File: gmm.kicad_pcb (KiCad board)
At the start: 6 copper layers, 55 x 50 mm, 14 parts, among them P1 10144518-101802LF, P2 10144518-061802LF, P3 10144518-061802LF, P4 10144518-061802LF, U1 CCGM1A1, U2 5P49V6965, U3 LM26480SQ, Y1 NX3225SA

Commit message: FPGA core and IO power, PLL and SERDES, FPGA GPIO signals are connected... WIP
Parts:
- added C10: 0.01uF, Capacitor_SMD:C_0402_1005Metric, F.Cu at (156.8, 171.9)
- added C11: 0.01uF, Capacitor_SMD:C_0402_1005Metric, F.Cu at (168.9, 161.9)
- added C12: 1.0uF, Capacitor_SMD:C_0603_1608Metric, F.Cu at (157.4, 164.7)
- added C13: 0.1uF, Capacitor_SMD:C_0402_1005Metric, F.Cu at (163.8, 166.9)
- added C14: 0.1uF, Capacitor_SMD:C_0402_1005Metric, F.Cu at (160.8, 168.9)
- added C15: 1.0uF, Capacitor_SMD:C_0603_1608Metric, F.Cu at (157.4, 162.2)
- added C16: 0.01uF, Capacitor_SMD:C_0402_1005Metric, F.Cu at (160.8, 170.9)
- added C17: 0.01uF, Capacitor_SMD:C_0402_1005Metric, F.Cu at (167.8, 164.4)
- added C18: 1.0uF, Capacitor_SMD:C_0603_1608Metric, F.Cu at (153.4, 162.2)
- added C19: 0.1uF, Capacitor_SMD:C_0402_1005Metric, F.Cu at (166.7, 168.4)
- added C20: 0.1uF, Capacitor_SMD:C_0402_1005Metric, F.Cu at (164.8, 164.4)
- added C21: 0.1uF, Capacitor_SMD:C_0402_1005Metric, F.Cu at (169.6, 171.8)
- added C22: 1.0uF, Capacitor_SMD:C_0603_1608Metric, F.Cu at (153.4, 156.2)
- added C23: 0.01uF, Capacitor_SMD:C_0402_1005Metric, F.Cu at (168.9, 145.9)
- added C24: 0.01uF, Capacitor_SMD:C_0402_1005Metric, F.Cu at (160.8, 153.5)
- added C25: 0.01uF, Capacitor_SMD:C_0402_1005Metric, F.Cu at (176.9, 138.4)
- added C26: 0.01uF, Capacitor_SMD:C_0402_1005Metric, F.Cu at (156.8, 156.0)
- added C27: 0.01uF, Capacitor_SMD:C_0402_1005Metric, F.Cu at (164.8, 148.5)
- added C28: 0.01uF, Capacitor_SMD:C_0402_1005Metric, F.Cu at (172.5, 152.9)
- added C29: 0.01uF, Capacitor_SMD:C_0402_1005Metric, F.Cu at (185.2, 146.4)
- added C3: 0.1uF, Capacitor_SMD:C_0402_1005Metric, F.Cu at (172.5, 167.9)
- added C30: 0.01uF, Capacitor_SMD:C_0402_1005Metric, F.Cu at (174.3, 156.8)
- added C31: 1.0uF, Capacitor_SMD:C_0603_1608Metric, F.Cu at (157.4, 153.7)
- added C32: 1.0uF, Capacitor_SMD:C_0603_1608Metric, F.Cu at (169.4, 143.7)
- added C33: 0.01uF, Capacitor_SMD:C_0402_1005Metric, F.Cu at (178.3, 152.9)
- added C34: 0.01uF, Capacitor_SMD:C_0402_1005Metric, F.Cu at (184.5, 142.4)
- added C35: 0.01uF, Capacitor_SMD:C_0402_1005Metric, F.Cu at (182.3, 148.4)
- added C36: 0.01uF, Capacitor_SMD:C_0402_1005Metric, F.Cu at (179.4, 150.4)
- added C37: 0.01uF, Capacitor_SMD:C_0402_1005Metric, F.Cu at (171.4, 156.8)
- added C38: 0.01uF, Capacitor_SMD:C_0402_1005Metric, F.Cu at (172.9, 140.9)
- added C39: 0.01uF, Capacitor_SMD:C_0402_1005Metric, F.Cu at (184.5, 144.4)
- added C4: 1.0uF, Capacitor_SMD:C_0603_1608Metric, F.Cu at (161.4, 162.2)
- added C40: 0.01uF, Capacitor_SMD:C_0402_1005Metric, F.Cu at (175.4, 152.9)
- added C41: 1.0uF, Capacitor_SMD:C_0603_1608Metric, F.Cu at (153.4, 151.2)
- added C42: 1.0uF, Capacitor_SMD:C_0603_1608Metric, F.Cu at (165.4, 141.2)
- added C43: 0.01uF, Capacitor_SMD:C_0402_1005Metric, F.Cu at (176.5, 150.9)
- added C44: 0.01uF, Capacitor_SMD:C_0402_1005Metric, F.Cu at (172.5, 154.9)
- added C45: 0.01uF, Capacitor_SMD:C_0402_1005Metric, F.Cu at (175.4, 154.9)
- added C46: 0.01uF, Capacitor_SMD:C_0402_1005Metric, F.Cu at (179.4, 146.4)
- added C47: 0.01uF, Capacitor_SMD:C_0402_1005Metric, F.Cu at (175.8, 142.9)
- added C48: 0.01uF, Capacitor_SMD:C_0402_1005Metric, F.Cu at (178.7, 142.4)
- added C49: 0.01uF, Capacitor_SMD:C_0402_1005Metric, F.Cu at (166.7, 154.4)
- added C5: 0.01uF, Capacitor_SMD:C_0402_1005Metric, F.Cu at (170.7, 163.9)
- added C50: 0.01uF, Capacitor_SMD:C_0402_1005Metric, F.Cu at (182.7, 138.4)
- added C51: 1.0uF, Capacitor_SMD:C_0603_1608Metric, F.Cu at (165.4, 146.2)
- added C52: 1.0uF, Capacitor_SMD:C_0603_1608Metric, F.Cu at (161.4, 151.2)
- added C53: 0.01uF, Capacitor_SMD:C_0402_1005Metric, F.Cu at (166.7, 152.4)
- added C54: 0.01uF, Capacitor_SMD:C_0402_1005Metric, F.Cu at (178.7, 140.4)
- added C55: 0.01uF, Capacitor_SMD:C_0402_1005Metric, F.Cu at (170.7, 147.9)
- added C56: 0.01uF, Capacitor_SMD:C_0402_1005Metric, F.Cu at (162.7, 155.5)
- added C57: 0.01uF, Capacitor_SMD:C_0402_1005Metric, F.Cu at (167.8, 150.4)
- added C58: 0.01uF, Capacitor_SMD:C_0402_1005Metric, F.Cu at (172.9, 142.9)
- added C59: 0.01uF, Capacitor_SMD:C_0402_1005Metric, F.Cu at (172.9, 144.9)
- added C6: 0.01uF, Capacitor_SMD:C_0402_1005Metric, F.Cu at (166.7, 166.4)
- added C60: 0.01uF, Capacitor_SMD:C_0402_1005Metric, F.Cu at (179.8, 138.4)
- added C61: 1.0uF, Capacitor_SMD:C_0603_1608Metric, F.Cu at (157.4, 143.7)
- added C62: 0.01uF, Capacitor_SMD:C_0402_1005Metric, F.Cu at (163.8, 153.5)
- added C63: 0.01uF, Capacitor_SMD:C_0402_1005Metric, F.Cu at (175.8, 140.9)
- added C64: 0.01uF, Capacitor_SMD:C_0402_1005Metric, F.Cu at (164.8, 150.4)
- added C65: 0.01uF, Capacitor_SMD:C_0402_1005Metric, F.Cu at (167.8, 148.5)
- added C66: 1.0uF, Capacitor_SMD:C_0603_1608Metric, F.Cu at (169.4, 138.7)
- added C67: 1.0uF, Capacitor_SMD:C_0603_1608Metric, F.Cu at (153.4, 153.7)
- added C68: 1.0uF, Capacitor_SMD:C_0603_1608Metric, F.Cu at (161.4, 146.2)
- added C69: 1.0uF, Capacitor_SMD:C_0603_1608Metric, F.Cu at (157.4, 148.7)
- added C7: 0.01uF, Capacitor_SMD:C_0402_1005Metric, F.Cu at (171.8, 161.9)
- added C70: 1.0uF, Capacitor_SMD:C_0603_1608Metric, F.Cu at (157.4, 146.2)
- added C71: 0.1uF, Capacitor_SMD:C_0402_1005Metric, F.Cu at (159.7, 156.0)
- added C72: 1.0uF, Capacitor_SMD:C_0603_1608Metric, F.Cu at (161.4, 148.7)
- added C73: 0.01uF, Capacitor_SMD:C_0402_1005Metric, F.Cu at (179.4, 148.4)
- added C74: 0.01uF, Capacitor_SMD:C_0402_1005Metric, F.Cu at (168.5, 156.4)
- added C75: 0.01uF, Capacitor_SMD:C_0402_1005Metric, F.Cu at (184.5, 140.4)
- added C76: 0.01uF, Capacitor_SMD:C_0402_1005Metric, F.Cu at (165.6, 156.4)
- added C77: 0.01uF, Capacitor_SMD:C_0402_1005Metric, F.Cu at (178.7, 144.4)
- added C78: 0.1uF, Capacitor_SMD:C_0402_1005Metric, F.Cu at (173.6, 148.9)
- added C79: 1.0uF, Capacitor_SMD:C_0603_1608Metric, F.Cu at (169.4, 141.2)
- added C8: 0.1uF, Capacitor_SMD:C_0402_1005Metric, F.Cu at (160.8, 166.9)
- added C80: 0.01uF, Capacitor_SMD:C_0402_1005Metric, F.Cu at (169.6, 152.4)
- added C81: 0.01uF, Capacitor_SMD:C_0402_1005Metric, F.Cu at (185.6, 138.4)
- added C82: 0.01uF, Capacitor_SMD:C_0402_1005Metric, F.Cu at (170.7, 149.9)
- added C83: 0.01uF, Capacitor_SMD:C_0402_1005Metric, F.Cu at (181.6, 142.4)
- added C84: 0.01uF, Capacitor_SMD:C_0402_1005Metric, F.Cu at (176.5, 146.9)
- added C85: 0.1uF, Capacitor_SMD:C_0402_1005Metric, F.Cu at (173.6, 150.9)
- added C86: 1.0uF, Capacitor_SMD:C_0603_1608Metric, F.Cu at (173.4, 138.7)
- added C87: 0.01uF, Capacitor_SMD:C_0402_1005Metric, F.Cu at (176.5, 148.9)
- added C88: 0.01uF, Capacitor_SMD:C_0402_1005Metric, F.Cu at (181.6, 144.4)
- added C89: 0.01uF, Capacitor_SMD:C_0402_1005Metric, F.Cu at (182.3, 146.4)
- added C9: 1.0uF, Capacitor_SMD:C_0603_1608Metric, F.Cu at (153.4, 164.7)
- added C90: 0.01uF, Capacitor_SMD:C_0402_1005Metric, F.Cu at (181.6, 140.4)
- added C91: 0.01uF, Capacitor_SMD:C_0402_1005Metric, F.Cu at (169.6, 154.4)
- added C92: 0.1uF, Capacitor_SMD:C_0402_1005Metric, F.Cu at (175.8, 144.9)
- added C93: 1.0uF, Capacitor_SMD:C_0603_1608Metric, F.Cu at (161.4, 143.7)
- added C94: 0.01uF, Capacitor_SMD:C_0402_1005Metric, F.Cu at (173.6, 146.9)
- added L1: 4.7uH, Inductor_SMD:L_0603_1608Metric, F.Cu at (153.4, 167.2)
- added L2: 4.7uH, Inductor_SMD:L_0603_1608Metric, F.Cu at (157.4, 169.7)
- added L3: 4.7uH, Inductor_SMD:L_0603_1608Metric, F.Cu at (165.4, 162.2)
- added L4: 4.7uH, Inductor_SMD:L_0603_1608Metric, F.Cu at (153.4, 172.2)
- added L5: 4.7uH, Inductor_SMD:L_0603_1608Metric, F.Cu at (161.4, 164.7)
- added L6: 4.7uH, Inductor_SMD:L_0603_1608Metric, F.Cu at (153.4, 148.7)
- added L7: 4.7uH, Inductor_SMD:L_0603_1608Metric, F.Cu at (161.4, 141.2)
- added L8: 4.7uH, Inductor_SMD:L_0603_1608Metric, F.Cu at (157.4, 151.2)
- added L9: 4.7uH, Inductor_SMD:L_0603_1608Metric, F.Cu at (153.4, 146.2)
- added R1: DNI, Resistor_SMD:R_0603_1608Metric, F.Cu at (157.4, 167.2)
- added R10: DNI, Resistor_SMD:R_0603_1608Metric, F.Cu at (161.4, 138.7)
- added R11: DNI, Resistor_SMD:R_0603_1608Metric, F.Cu at (157.4, 141.2)
- added R12: DNI, Resistor_SMD:R_0603_1608Metric, F.Cu at (153.4, 143.7)
- added R13: DNI, Resistor_SMD:R_0603_1608Metric, F.Cu at (157.4, 138.7)
- added R14: DNI, Resistor_SMD:R_0603_1608Metric, F.Cu at (153.4, 141.2)
- added R15: DNI, Resistor_SMD:R_0603_1608Metric, F.Cu at (165.4, 138.7)
- added R16: DNI, Resistor_SMD:R_0603_1608Metric, F.Cu at (165.4, 143.7)
- added R17: DNI, Resistor_SMD:R_0603_1608Metric, F.Cu at (153.4, 138.7)
- added R2: DNI, Resistor_SMD:R_0603_1608Metric, F.Cu at (153.4, 169.7)
- added R3: 33, Resistor_SMD:R_0402_1005Metric, F.Cu at (163.8, 168.9)
- added R4: 100, Resistor_SMD:R_0402_1005Metric, F.Cu at (163.8, 170.9)
- added R5: 10k, Resistor_SMD:R_0402_1005Metric, F.Cu at (170.7, 165.9)
- added R6: DNI, Resistor_SMD:R_0402_1005Metric, F.Cu at (166.7, 170.4)
- added R7: 200, Resistor_SMD:R_0402_1005Metric, F.Cu at (169.6, 167.9)
- added R8: 10k, Resistor_SMD:R_0402_1005Metric, F.Cu at (169.6, 169.9)
- added R9: 10k, Resistor_SMD:R_0402_1005Metric, F.Cu at (166.7, 172.4)
- MH1, MH2, MH3, MH4: footprint Mounting_Holes:MountingHole_2.7mm_M2.5_ISO14580_Pad -> MountingHole:MountingHole_2.7mm_M2.5_ISO14580_Pad
- P1: value 10144518-101802LF -> 10144518-061802LF; footprint Amphenol:10144518-101802LF -> Amphenol:10144518-061802LF; moved to F.Cu
- P2, P3: moved to F.Cu
- P4: value 10144518-061802LF -> 10144518-101802LF; footprint Amphenol:10144518-061802LF -> Amphenol:10144518-101802LF; moved to F.Cu
- U2: footprint Housings_DFN_QFN:QFN-24-1EP_4x4mm_Pitch0.5mm -> Package_DFN_QFN:QFN-24-1EP_4x4mm_P0.5mm_EP2.8x2.8mm_ThermalVias
- moved MH2 113.2 mm to (88.0, 182.5)
- moved MH1 106.3 mm to (88.0, 188.5)
- moved MH3 85.9 mm to (82.0, 188.5)
- moved P2 69.8 mm to (128.5, 153.3)
- moved P3 66.4 mm to (95.5, 153.3), turned to 0 degrees
- moved MH4 58.7 mm to (82.0, 182.5)
- moved P1 58.1 mm to (95.5, 163.7), turned to 0 degrees
- moved P4 23.7 mm to (103.4, 143.0), turned to 0 degrees
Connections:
- U1 pad A2: (no net) -> /Clock and SERDES/TXC_N
- U1 pad A3: (no net) -> /Clock and SERDES/TXC_P
- U1 pad A7: (no net) -> VIO_N1
- U1 pad B12: (no net) -> VIO_N2
- U1 pad B17: (no net) -> VIO_E2
- U1 pad B2: (no net) -> Net-(R7-Pad2)
- U1 pad B3: (no net) -> Net-(C79-Pad1)
- U1 pad C2: (no net) -> Net-(C72-Pad1)
- U1 pad C6: (no net) -> VIO_N1
- U1 pad D12: (no net) -> VIO_N2
- U1 pad D2: (no net) -> /Clock and SERDES/CLK_P
- U1 pad E1: (no net) -> /Clock and SERDES/CLK_N
- U1 pad E11: (no net) -> VIO_N2
- U1 pad E14: (no net) -> VIO_N2
- U1 pad E16: (no net) -> VIO_E2
- U1 pad E18: (no net) -> VIO_E2
- U1 pad E4: (no net) -> Net-(C93-Pad1)
- U1 pad E5: (no net) -> Net-(C86-Pad1)
- U1 pad E7: (no net) -> VIO_N1
- U1 pad E9: (no net) -> VIO_N1
- U1 pad F10: (no net) -> +1V0
- U1 pad F12: (no net) -> VIO_N2
- U1 pad F8: (no net) -> VIO_N1
- U1 pad G11: (no net) -> +1V0
- U1 pad G13: (no net) -> VIO_E2
- U1 pad G14: (no net) -> VIO_E2
- U1 pad G5: (no net) -> VIO_W2
- U1 pad G7: (no net) -> +1V0
- U1 pad G9: (no net) -> +1V0
- U1 pad H10: (no net) -> +1V0
- U1 pad H12: (no net) -> +1V0
- U1 pad H2: (no net) -> VIO_W2
- U1 pad H4: (no net) -> VIO_W2
- U1 pad H6: (no net) -> VIO_W2
- U1 pad H8: (no net) -> +1V0
- U1 pad J11: (no net) -> +1V0
- U1 pad J13: (no net) -> +1V0
- U1 pad J14: (no net) -> VIO_E1
- U1 pad J5: (no net) -> VIO_W2
- U1 pad J7: (no net) -> +1V0
- U1 pad J9: (no net) -> +1V0
- U1 pad K10: (no net) -> +1V0
- U1 pad K12: (no net) -> +1V0
- U1 pad K15: (no net) -> VIO_E1
- U1 pad K17: (no net) -> VIO_E1
- U1 pad K6: (no net) -> +1V0
- U1 pad K8: (no net) -> +1V0
- U1 pad L11: (no net) -> +1V0
- U1 pad L13: (no net) -> VIO_E1
- U1 pad L5: (no net) -> VIO_W1
- U1 pad L7: (no net) -> +1V0
- U1 pad L9: (no net) -> +1V0
- U1 pad M10: (no net) -> +1V0
- U1 pad M12: (no net) -> +1V0
- U1 pad M13: (no net) -> VIO_S2
- U1 pad M14: (no net) -> VIO_E1
- U1 pad M5: (no net) -> VIO_W1
- U1 pad M6: (no net) -> VIO_W1
- U1 pad M8: (no net) -> +1V0
- U1 pad N11: (no net) -> VIO_S1
- U1 pad N14: (no net) -> VIO_S2
- U1 pad N7: (no net) -> +2V5
- U1 pad N9: (no net) -> +1V0
- U1 pad P10: (no net) -> VIO_S1
- U1 pad P12: (no net) -> VIO_S1
- U1 pad P13: (no net) -> VIO_S2
- U1 pad P2: (no net) -> VIO_W1
- U1 pad P4: (no net) -> VIO_W1
- U1 pad P8: (no net) -> +2V5
- U1 pad R11: (no net) -> VIO_S1
- U1 pad R17: (no net) -> VIO_S2
- U1 pad R6: (no net) -> +2V5
- U1 pad U11: (no net) -> VIO_S1
- U1 pad U17: (no net) -> VIO_S2
- U1 pad U3: (no net) -> +2V5
- U1 pad U6: (no net) -> +2V5
- U2 pad 1: (no net) -> CLKI_P
- U2 pad 10: (no net) -> Net-(C17-Pad1)
- U2 pad 15: (no net) -> Net-(C11-Pad1)
- U2 pad 18: (no net) -> Net-(C4-Pad1)
- U2 pad 19: (no net) -> /Clock and SERDES/CLK_N
- U2 pad 2: (no net) -> CLKI_N
- U2 pad 20: (no net) -> /Clock and SERDES/CLK_P
- U2 pad 21: (no net) -> Net-(C4-Pad1)
- U2 pad 22: (no net) -> Net-(C10-Pad1)
- U2 pad 23: (no net) -> Net-(C4-Pad1)
- U2 pad 24: (no net) -> Net-(R3-Pad2)
- U2 pad 25: Net-(U2-Pad25) -> GND
- U2 pad 5: (no net) -> Net-(C15-Pad1)
- U2 pad 6: (no net) -> CLKSEL
- U2 pad 7: (no net) -> CLKSDOE
- U3 pad 15: (no net) -> GND
- U3 pad 18: (no net) -> GND
- U3 pad 25: (no net) -> GND
- U3 pad 4: (no net) -> GND
- U3 pad 9: (no net) -> GND

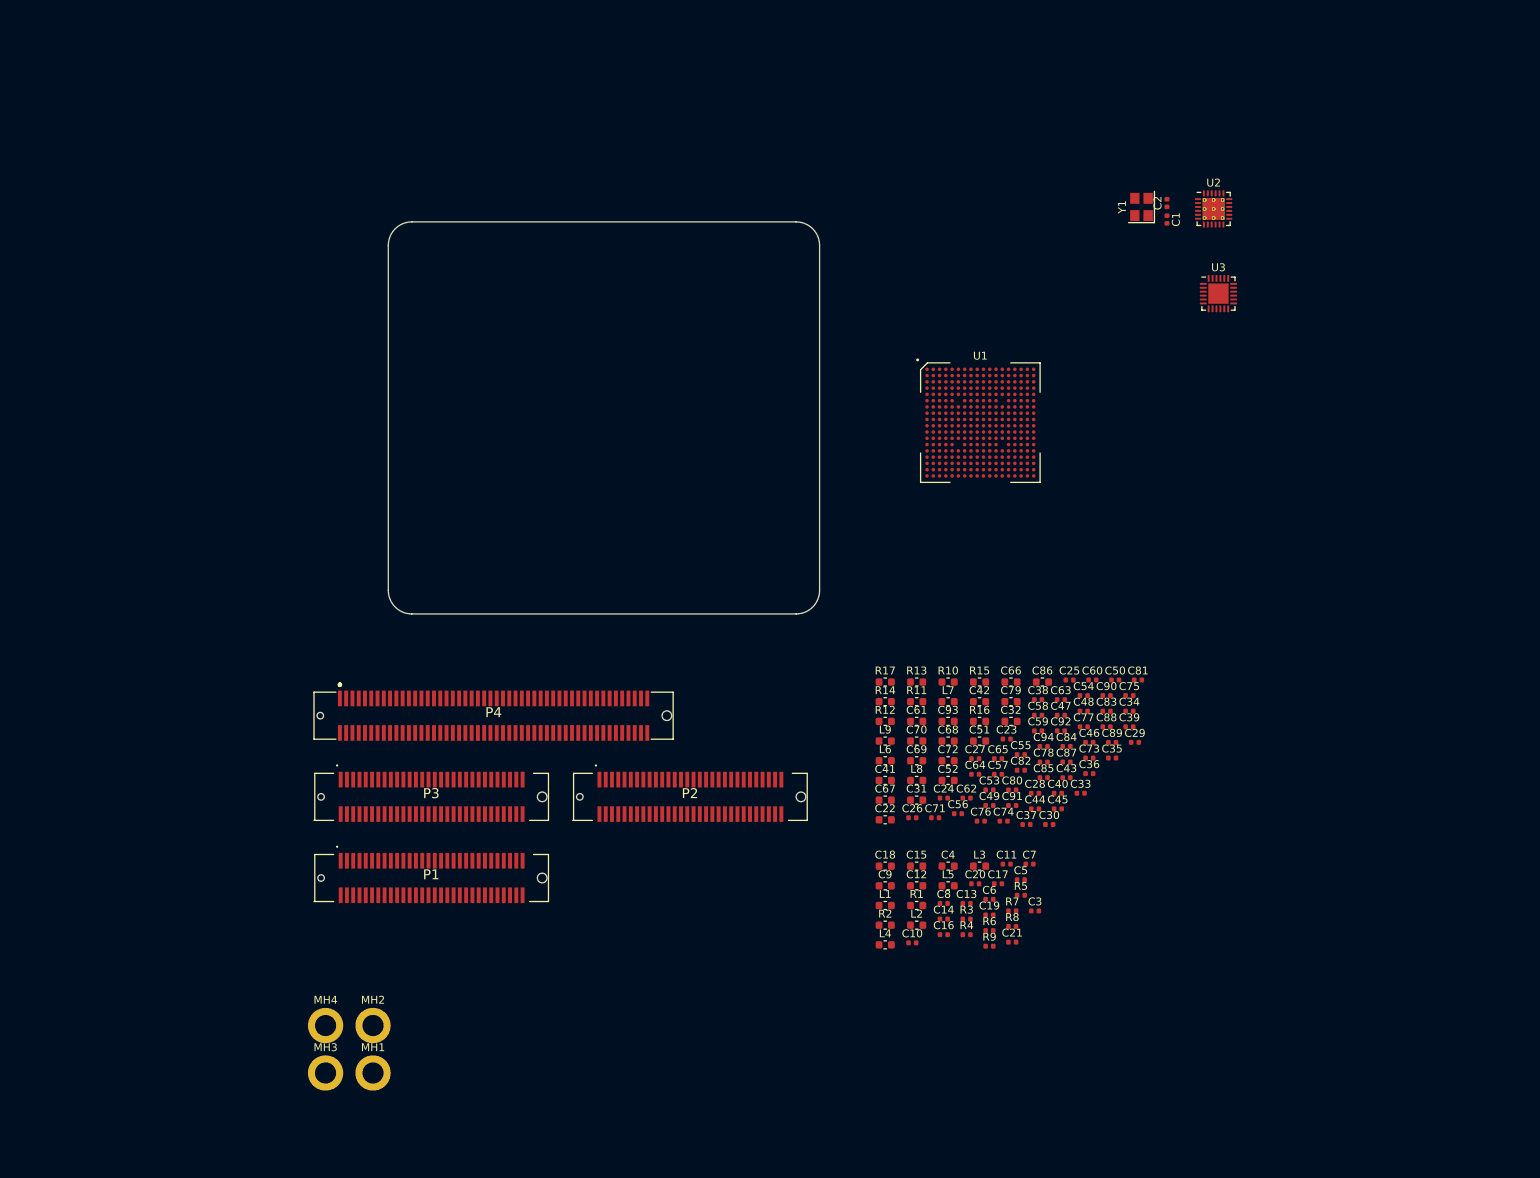
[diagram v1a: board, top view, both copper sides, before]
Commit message: Schematic is [almost] done.  TODO: Connectors and a few footprints
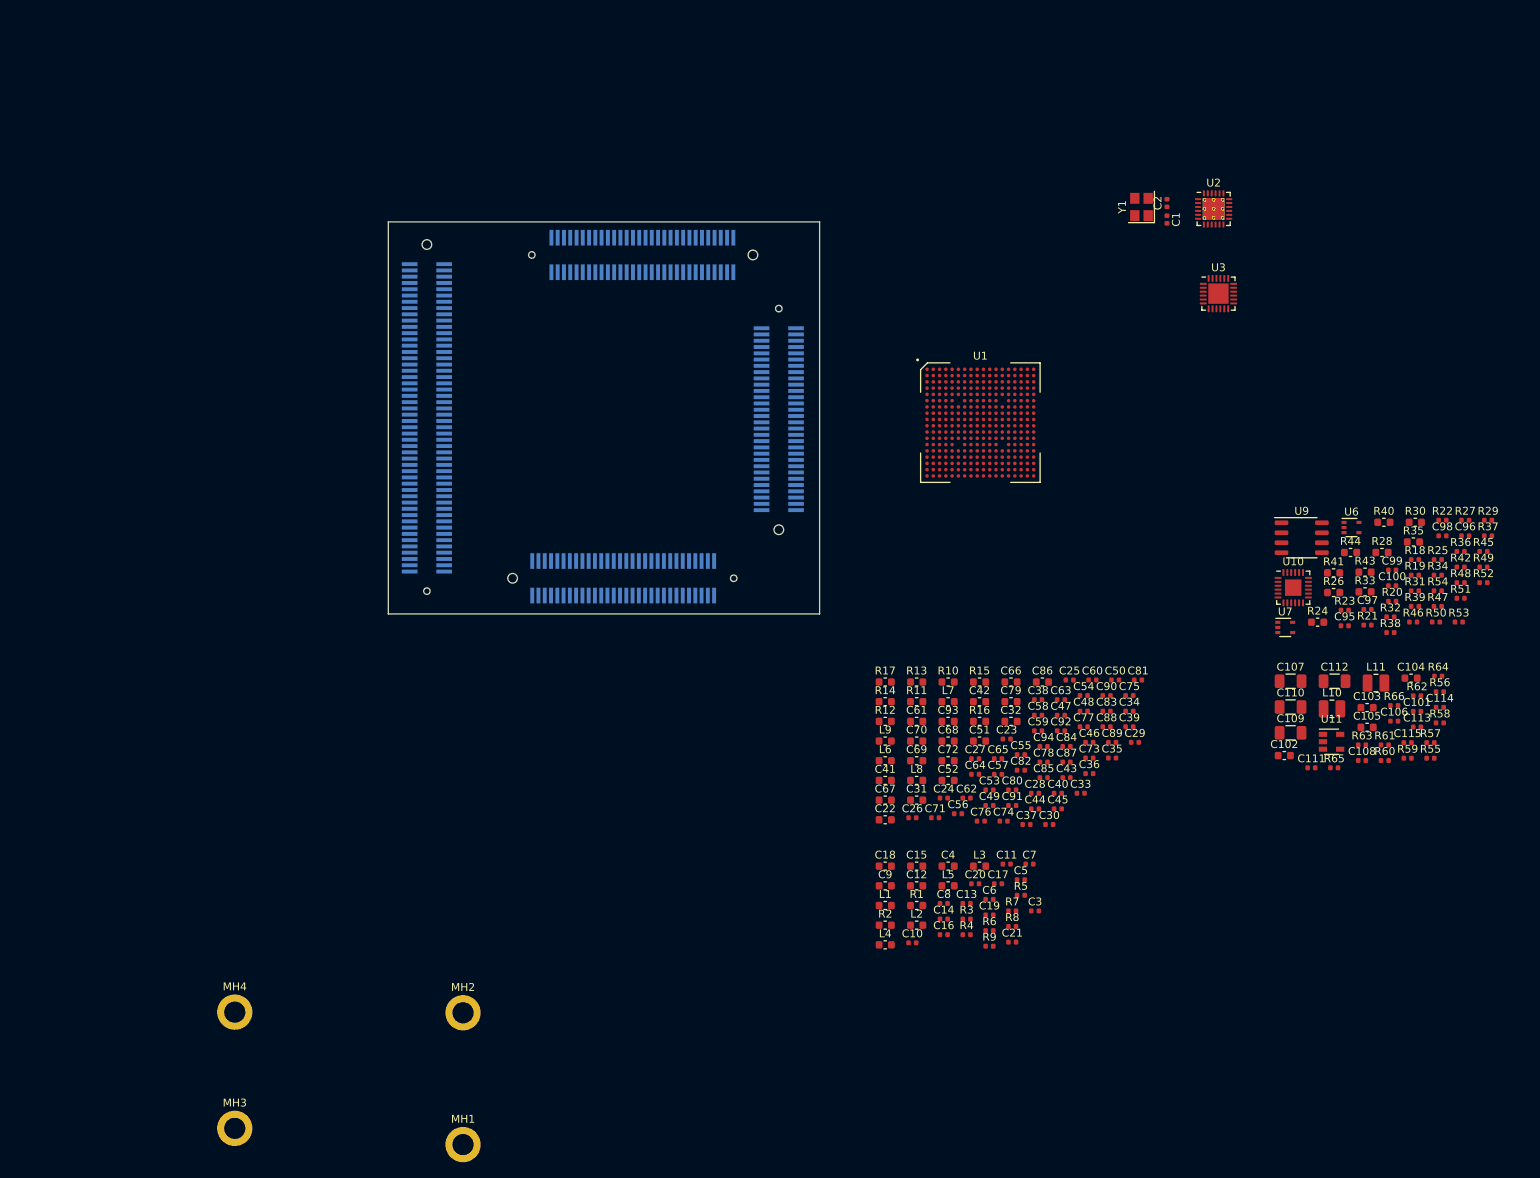
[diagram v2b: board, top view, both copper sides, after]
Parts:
- added C100: 0.1uF, Capacitor_SMD:C_0402_1005Metric, F.Cu at (218.0, 126.4)
- added C101: 0.1uF, Capacitor_SMD:C_0402_1005Metric, F.Cu at (221.2, 142.4)
- added C102: 1uF, Capacitor_SMD:C_0603_1608Metric, F.Cu at (204.3, 148.1)
- added C103: 1uF, Capacitor_SMD:C_0603_1608Metric, F.Cu at (214.8, 141.9)
- added C104: 1uF, Capacitor_SMD:C_0603_1608Metric, F.Cu at (220.4, 138.2)
- added C105: 1uF, Capacitor_SMD:C_0603_1608Metric, F.Cu at (214.8, 144.4)
- added C106: 15pF, Capacitor_SMD:C_0402_1005Metric, F.Cu at (218.3, 143.7)
- added C107: 10uF, Capacitor_SMD:C_1206_3216Metric, F.Cu at (205.1, 138.6)
- added C108: DNI, Capacitor_SMD:C_0402_1005Metric, F.Cu at (214.2, 148.7)
- added C109: 10uF, Capacitor_SMD:C_1206_3216Metric, F.Cu at (205.1, 145.2)
- added C110: 10uF, Capacitor_SMD:C_1206_3216Metric, F.Cu at (205.1, 141.9)
- added C111: 8.2pF, Capacitor_SMD:C_0402_1005Metric, F.Cu at (207.7, 149.6)
- added C112: 10uF, Capacitor_SMD:C_1206_3216Metric, F.Cu at (210.7, 138.6)
- added C113: DNI, Capacitor_SMD:C_0402_1005Metric, F.Cu at (221.2, 144.4)
- added C114: 0.47uF, Capacitor_SMD:C_0402_1005Metric, F.Cu at (224.1, 141.9)
- added C115: 0.47uF, Capacitor_SMD:C_0402_1005Metric, F.Cu at (220.0, 146.4)
- added C95: 0.1uF, Capacitor_SMD:C_0402_1005Metric, F.Cu at (212.0, 131.5)
- added C96: 0.1uF, Capacitor_SMD:C_0402_1005Metric, F.Cu at (227.3, 120.0)
- added C97: 0.1uF, Capacitor_SMD:C_0402_1005Metric, F.Cu at (214.9, 129.4)
- added C98: 0.1uF, Capacitor_SMD:C_0402_1005Metric, F.Cu at (224.4, 120.0)
- added C99: 0.1uF, Capacitor_SMD:C_0402_1005Metric, F.Cu at (218.0, 124.4)
- added L10: 2.2uH, Inductor_SMD:L_1008_2520Metric, F.Cu at (210.3, 142.1)
- added L11: 2.2uH, Inductor_SMD:L_1008_2520Metric, F.Cu at (215.9, 138.8)
- added R18: 10k, Resistor_SMD:R_0402_1005Metric, F.Cu at (220.9, 123.1)
- added R19: 100k, Resistor_SMD:R_0402_1005Metric, F.Cu at (220.9, 125.1)
- added R20: 10k, Resistor_SMD:R_0402_1005Metric, F.Cu at (218.0, 128.4)
- added R21: 10k, Resistor_SMD:R_0402_1005Metric, F.Cu at (214.9, 131.4)
- added R22: 33, Resistor_SMD:R_0402_1005Metric, F.Cu at (224.4, 118.0)
- added R23: 1k, Resistor_SMD:R_0402_1005Metric, F.Cu at (212.0, 129.5)
- added R24: 10k, Resistor_SMD:R_0603_1608Metric, F.Cu at (208.5, 131.1)
- added R25: 33, Resistor_SMD:R_0402_1005Metric, F.Cu at (223.8, 123.1)
- added R26: DNI, Resistor_SMD:R_0603_1608Metric, F.Cu at (210.6, 127.3)
- added R27: DNI, Resistor_SMD:R_0402_1005Metric, F.Cu at (227.3, 118.0)
- added R28: 100k, Resistor_SMD:R_0603_1608Metric, F.Cu at (216.7, 122.2)
- added R29: 33, Resistor_SMD:R_0402_1005Metric, F.Cu at (230.2, 118.0)
- added R30: 100k, Resistor_SMD:R_0603_1608Metric, F.Cu at (221.0, 118.3)
- added R31: 33, Resistor_SMD:R_0402_1005Metric, F.Cu at (220.9, 127.0)
- added R32: 33, Resistor_SMD:R_0402_1005Metric, F.Cu at (217.8, 130.4)
- added R33: 100k, Resistor_SMD:R_0603_1608Metric, F.Cu at (214.6, 127.2)
- added R34: 33, Resistor_SMD:R_0402_1005Metric, F.Cu at (223.8, 125.1)
- added R35: 10k, Resistor_SMD:R_0603_1608Metric, F.Cu at (220.7, 120.8)
- added R36: 33, Resistor_SMD:R_0402_1005Metric, F.Cu at (226.8, 122.0)
- added R37: 4.7k, Resistor_SMD:R_0402_1005Metric, F.Cu at (230.2, 120.0)
- added R38: 4.7k, Resistor_SMD:R_0402_1005Metric, F.Cu at (217.8, 132.4)
- added R39: 4.7k, Resistor_SMD:R_0402_1005Metric, F.Cu at (220.9, 129.0)
- added R40: 10k, Resistor_SMD:R_0603_1608Metric, F.Cu at (217.0, 118.3)
- added R41: 10k, Resistor_SMD:R_0603_1608Metric, F.Cu at (210.6, 124.8)
- added R42: 33, Resistor_SMD:R_0402_1005Metric, F.Cu at (226.8, 124.0)
- added R43: 100k, Resistor_SMD:R_0603_1608Metric, F.Cu at (214.6, 124.7)
- added R44: 100k, Resistor_SMD:R_0603_1608Metric, F.Cu at (212.7, 122.2)
- added R45: 10k, Resistor_SMD:R_0402_1005Metric, F.Cu at (229.7, 122.0)
- added R46: 10k, Resistor_SMD:R_0402_1005Metric, F.Cu at (220.7, 131.0)
- added R47: 10k, Resistor_SMD:R_0402_1005Metric, F.Cu at (223.8, 129.0)
- added R48: 10k, Resistor_SMD:R_0402_1005Metric, F.Cu at (226.8, 126.0)
- added R49: 10k, Resistor_SMD:R_0402_1005Metric, F.Cu at (229.7, 124.0)
- added R50: 10k, Resistor_SMD:R_0402_1005Metric, F.Cu at (223.6, 131.0)
- added R51: 10k, Resistor_SMD:R_0402_1005Metric, F.Cu at (226.8, 128.0)
- added R52: 10k, Resistor_SMD:R_0402_1005Metric, F.Cu at (229.7, 126.0)
- added R53: 10k, Resistor_SMD:R_0402_1005Metric, F.Cu at (226.5, 131.0)
- added R54: 10k, Resistor_SMD:R_0402_1005Metric, F.Cu at (223.8, 127.0)
- added R55: 10k, Resistor_SMD:R_0402_1005Metric, F.Cu at (222.9, 148.4)
- added R56: 10k, Resistor_SMD:R_0402_1005Metric, F.Cu at (224.1, 139.9)
- added R57: 100k, Resistor_SMD:R_0402_1005Metric, F.Cu at (222.9, 146.4)
- added R58: 100k, Resistor_SMD:R_0402_1005Metric, F.Cu at (224.1, 143.9)
- added R59: 10k, Resistor_SMD:R_0402_1005Metric, F.Cu at (220.0, 148.4)
- added R60: 402k, Resistor_SMD:R_0402_1005Metric, F.Cu at (217.1, 148.7)
- added R61: 100k, Resistor_SMD:R_0402_1005Metric, F.Cu at (217.1, 146.7)
- added R62: 10k, Resistor_SMD:R_0402_1005Metric, F.Cu at (221.2, 140.4)
- added R63: 100k, Resistor_SMD:R_0402_1005Metric, F.Cu at (214.2, 146.7)
- added R64: 100k, Resistor_SMD:R_0402_1005Metric, F.Cu at (223.9, 137.9)
- added R65: 100k, Resistor_SMD:R_0402_1005Metric, F.Cu at (210.6, 149.6)
- added R66: 100k, Resistor_SMD:R_0402_1005Metric, F.Cu at (218.3, 141.7)
- added U10: PCA9539AHF, Package_DFN_QFN:Texas_S-PVQFN-N24_EP2.1x2.1mm, F.Cu at (205.4, 126.7)
- added U11: TPS3840DL28DBV, Package_TO_SOT_SMD:SOT-23-5, F.Cu at (210.3, 146.3)
- added U6: 74LVC1G08, Package_TO_SOT_SMD:SOT-353_SC-70-5, F.Cu at (212.8, 119.0)
- added U7: 74LVC1G07, Package_TO_SOT_SMD:SOT-353_SC-70-5, F.Cu at (204.4, 131.7)
- added U9: IS25LQ032B-JNLE, Package_SO:SO-8_3.9x4.9mm_P1.27mm, F.Cu at (206.5, 120.3)
- P1, P2, P3, P4: moved to B.Cu
- moved P1 83.9 mm to (122.4, 84.2)
- moved P2 49.5 mm to (139.8, 105.2), turned to 270 degrees
- moved P4 38.9 mm to (94.9, 105.0), turned to 90 degrees
- moved P3 37.1 mm to (120.0, 125.5), turned to 180 degrees
- moved MH1 14.7 mm to (99.5, 197.7)
- moved MH3 13.6 mm to (70.4, 195.6)
- moved MH4 11.7 mm to (70.4, 180.8)
- moved MH2 11.6 mm to (99.5, 180.9)
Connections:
- U1 pad C3: (no net) -> Net-(C97-Pad1)
- U1 pad D4: (no net) -> Net-(U1-PadD4)
- U1 pad R7: (no net) -> JTAG_TCK
- U1 pad T3: (no net) -> /Configuration and Control/CFG_MD0
- U1 pad T4: (no net) -> /Configuration and Control/CFG_MD1
- U1 pad T5: (no net) -> JTAG_TDI
- U1 pad T7: (no net) -> Net-(R25-Pad2)
- U1 pad U1: (no net) -> /Configuration and Control/CFG_MD2
- U1 pad U2: (no net) -> /Configuration and Control/CFG_MD3
- U1 pad U5: (no net) -> JTAG_TMS
- U1 pad V2: (no net) -> CFG_FAILED_N
- U1 pad V3: (no net) -> CFG_DONE
- U1 pad V4: (no net) -> /Configuration and Control/POR_EN
- U1 pad V5: (no net) -> Net-(R22-Pad1)
- U2 pad 8: (no net) -> SDA
- U2 pad 9: (no net) -> SCL
- U3 pad 1: (no net) -> V_IN
- U3 pad 10: (no net) -> V_IN
- U3 pad 11: (no net) -> Net-(C111-Pad2)
- U3 pad 12: (no net) -> OFF_N
- U3 pad 13: (no net) -> V_IN
- U3 pad 14: (no net) -> Net-(L11-Pad1)
- U3 pad 16: (no net) -> Net-(R62-Pad2)
- U3 pad 17: (no net) -> Net-(R62-Pad2)
- U3 pad 19: (no net) -> +2V5
- U3 pad 2: (no net) -> GND
- U3 pad 20: (no net) -> V_1P0_A1
- U3 pad 21: (no net) -> Net-(R63-Pad2)
- U3 pad 22: (no net) -> Net-(R65-Pad2)
- U3 pad 23: (no net) -> V_1P0_A2
- U3 pad 24: (no net) -> +2V5
- U3 pad 3: (no net) -> POR_N
- U3 pad 5: (no net) -> Net-(L10-Pad1)
- U3 pad 6: (no net) -> V_IN
- U3 pad 7: (no net) -> OFF_N
- U3 pad 8: (no net) -> Net-(C106-Pad2)
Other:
- outline, holes or cut-outs redrawn

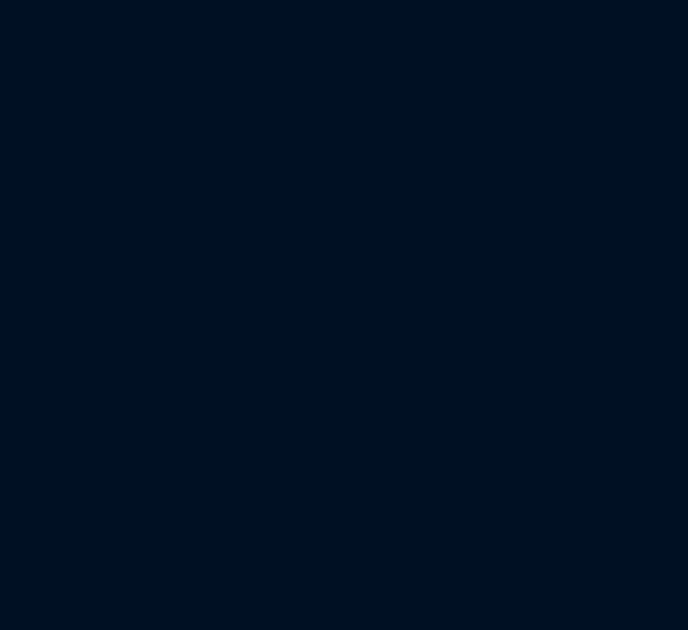
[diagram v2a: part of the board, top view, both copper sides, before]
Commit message: Footprint for high bandwidth quad SPDT switch (STmicro STG3692) is created.
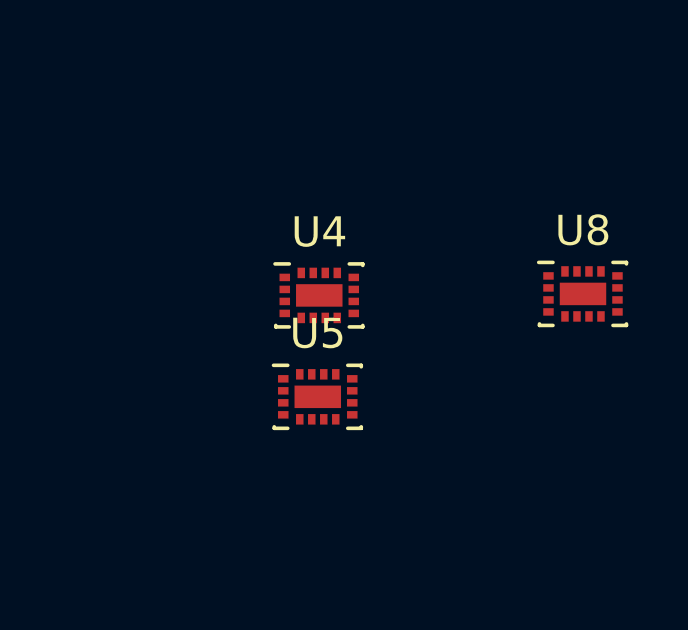
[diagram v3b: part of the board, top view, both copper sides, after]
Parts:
- added U4: STG3692, gmm:QFN-16-1EP_2.6x1.8mm_P0.4mm_EP1.5x0.7mm, F.Cu at (224.6, 97.3)
- added U5: STG3692, gmm:QFN-16-1EP_2.6x1.8mm_P0.4mm_EP1.5x0.7mm, F.Cu at (224.5, 100.7)
- added U8: STG3692, gmm:QFN-16-1EP_2.6x1.8mm_P0.4mm_EP1.5x0.7mm, F.Cu at (233.4, 97.2)
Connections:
- U1 pad R8: (no net) -> /Configuration and Control/GM_SPI_D1
- U1 pad T8: (no net) -> /Configuration and Control/GM_SPI_D0
- U1 pad U7: (no net) -> /Configuration and Control/GM_SPI_D2
- U1 pad U8: (no net) -> /Configuration and Control/GM_SPI_CLK
- U1 pad V7: (no net) -> /Configuration and Control/GM_SPI_D3
- U1 pad V8: (no net) -> /Configuration and Control/GM_SPI_CS_N
- U9 pad 2: (no net) -> /Configuration and Control/NOR_D1
- U9 pad 5: (no net) -> /Configuration and Control/NOR_D0
- U9 pad 6: (no net) -> /Configuration and Control/NOR_CLK
